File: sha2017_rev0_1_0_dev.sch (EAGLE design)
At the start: 193 parts, among them IC1 CP210X_USB_UART, IC2 AP7215, IC3 ESP32WROOM32, IC4 MCP73833, IC5 FXL6408, IC6 CPT112, Q1 MOSFET-PCHANNEL, Q2 MMBT2222A, Q3 MMBT2222A, Q4 MMBT2222A, Q5 MMBT2222A, Q6 SI1304 BDL, Q7 MMBT2222A, Q8 MOSFET-PCHANNEL, T1 SI2301DS, X1 JST-PH3, X2 2908-05WB-MG

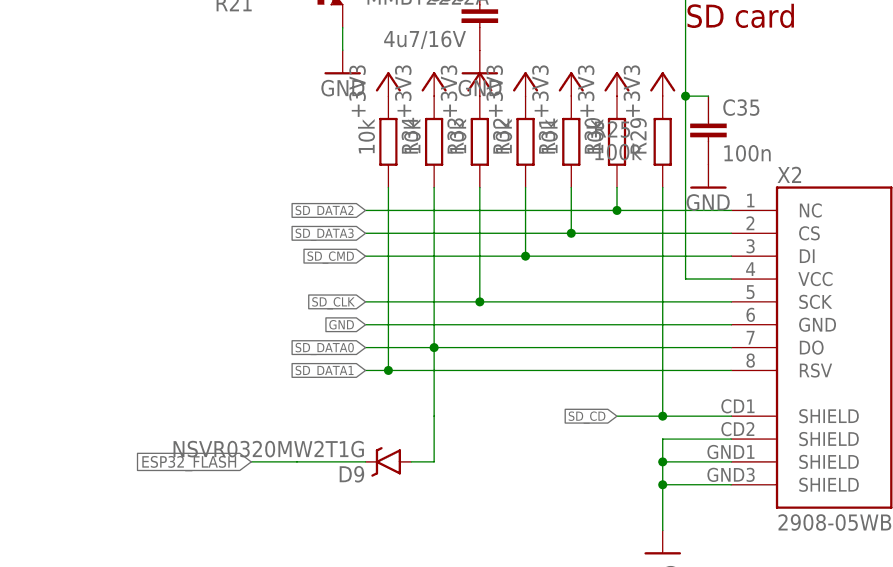
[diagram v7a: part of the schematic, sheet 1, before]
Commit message: add solder briges to unused IOs at 1 Wire SDiomode (roosted: MIMIMI I WANT MORE IOS!!!!!)
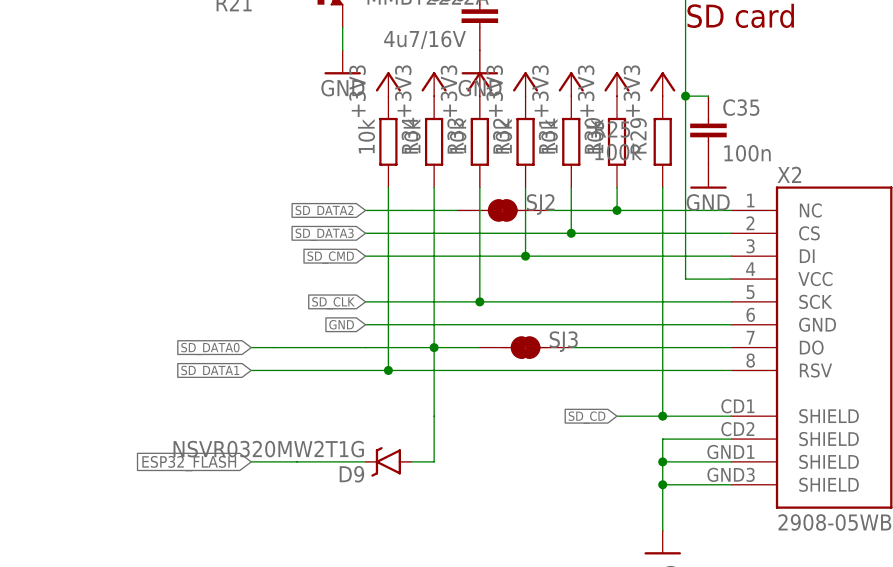
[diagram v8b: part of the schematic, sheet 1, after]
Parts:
- added SJ2, SJ3: JUMPER-PAD-2-NC_BY_TRACE, SparkFun-Passives:JUMPER-PAD-2-NC_BY_TRACE
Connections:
- new net N$20: SJ3.2, X2.DO
- new net SD_DATA2_OUT: R29.1, SJ2.2, X2.NC
- net SD_DATA0: now also SJ3.1; no longer X2.DO
- net SD_DATA2: now also SJ2.1; no longer R29.1, X2.NC
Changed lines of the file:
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@@
 <attribute name="PARTNO" value="BAT20JFILM"/>
 </part>
+<part name="SJ2" library="SparkFun-Passives" deviceset="JUMPER-PAD-2-NC_BY_TRACE" device=""/>
+<part name="SJ3" library="SparkFun-Passives" deviceset="JUMPER-PAD-2-NC_BY_TRACE" device=""/>
 </parts>
 <sheets>
@@
 <attribute name="PARTNO" x="129.54" y="33.02" size="1.778" layer="96" rot="MR270" display="off"/>
 </instance>
+<instance part="SJ2" gate="G$1" x="142.24" y="60.96" smashed="yes">
+<attribute name="NAME" x="144.78" y="60.96" size="1.778" layer="95"/>
+</instance>
+<instance part="SJ3" gate="G$1" x="144.78" y="45.72" smashed="yes">
+<attribute name="NAME" x="147.32" y="45.72" size="1.778" layer="95"/>
+</instance>
 </instances>
 <busses>
@@
 </segment>
 </net>
-<net name="SD_DATA2" class="0">
-<segment>
-<pinref part="X2" gate="G$1" pin="NC"/>
-<wire x1="167.64" y1="60.96" x2="154.94" y2="60.96" width="0.1524" layer="91"/>
-<label x="127" y="60.96" size="1.016" layer="95" rot="R180" xref="yes"/>
-<pinref part="R29" gate="G$1" pin="1"/>
-<wire x1="154.94" y1="60.96" x2="127" y2="60.96" width="0.1524" layer="91"/>
-<wire x1="154.94" y1="63.5" x2="154.94" y2="60.96" width="0.1524" layer="91"/>
-<junction x="154.94" y="60.96"/>
-</segment>
-</net>
 <net name="SD_DATA0" class="0">
 <segment>
-<pinref part="X2" gate="G$1" pin="DO"/>
-<wire x1="167.64" y1="45.72" x2="134.62" y2="45.72" width="0.1524" layer="91"/>
-<label x="127" y="45.72" size="1.016" layer="95" rot="R180" xref="yes"/>
+<wire x1="116.84" y1="45.72" x2="114.3" y2="45.72" width="0.1524" layer="91"/>
+<label x="114.3" y="45.72" size="1.016" layer="95" rot="R180" xref="yes"/>
 <pinref part="R33" gate="G$1" pin="1"/>
+<wire x1="139.7" y1="45.72" x2="134.62" y2="45.72" width="0.1524" layer="91"/>
 <wire x1="134.62" y1="45.72" x2="127" y2="45.72" width="0.1524" layer="91"/>
 <wire x1="134.62" y1="63.5" x2="134.62" y2="45.72" width="0.1524" layer="91"/>
@@
 <wire x1="132.08" y1="33.02" x2="134.62" y2="33.02" width="0.1524" layer="91"/>
 <wire x1="134.62" y1="33.02" x2="134.62" y2="38.1" width="0.1524" layer="91"/>
+<wire x1="116.84" y1="45.72" x2="127" y2="45.72" width="0.1524" layer="91"/>
+<pinref part="SJ3" gate="G$1" pin="1"/>
 </segment>
 </net>
 <net name="SD_DATA1" class="0">
 <segment>
+<wire x1="116.84" y1="43.18" x2="114.3" y2="43.18" width="0.1524" layer="91"/>
+<label x="114.3" y="43.18" size="1.016" layer="95" rot="R180" xref="yes"/>
 <pinref part="X2" gate="G$1" pin="RSV"/>
 <wire x1="167.64" y1="43.18" x2="129.54" y2="43.18" width="0.1524" layer="91"/>
-<label x="127" y="43.18" size="1.016" layer="95" rot="R180" xref="yes"/>
 <pinref part="R34" gate="G$1" pin="1"/>
 <wire x1="129.54" y1="43.18" x2="127" y2="43.18" width="0.1524" layer="91"/>
 <wire x1="129.54" y1="63.5" x2="129.54" y2="43.18" width="0.1524" layer="91"/>
 <junction x="129.54" y="43.18"/>
+<wire x1="116.84" y1="43.18" x2="127" y2="43.18" width="0.1524" layer="91"/>
 </segment>
 </net>
@@
 <pinref part="P+7" gate="VCC" pin="VCC"/>
 <pinref part="R1" gate="G$1" pin="2"/>
+</segment>
+</net>
+<net name="N$20" class="0">
+<segment>
+<pinref part="X2" gate="G$1" pin="DO"/>
+<wire x1="167.64" y1="45.72" x2="149.86" y2="45.72" width="0.1524" layer="91"/>
+<pinref part="SJ3" gate="G$1" pin="2"/>
+</segment>
+</net>
+<net name="SD_DATA2_OUT" class="0">
+<segment>
+<pinref part="X2" gate="G$1" pin="NC"/>
+<wire x1="167.64" y1="60.96" x2="154.94" y2="60.96" width="0.1524" layer="91"/>
+<pinref part="R29" gate="G$1" pin="1"/>
+<wire x1="154.94" y1="60.96" x2="147.32" y2="60.96" width="0.1524" layer="91"/>
+<wire x1="154.94" y1="63.5" x2="154.94" y2="60.96" width="0.1524" layer="91"/>
+<junction x="154.94" y="60.96"/>
+<pinref part="SJ2" gate="G$1" pin="2"/>
+</segment>
+</net>
+<net name="SD_DATA2" class="0">
+<segment>
+<pinref part="SJ2" gate="G$1" pin="1"/>
+<wire x1="137.16" y1="60.96" x2="132.08" y2="60.96" width="0.1524" layer="91"/>
+<wire x1="132.08" y1="60.96" x2="127" y2="60.96" width="0.1524" layer="91"/>
+<label x="127" y="60.96" size="1.016" layer="95" rot="R180" xref="yes"/>
 </segment>
 </net>
@@
 </segment>
 </net>
-<net name="SD_DATA2" class="0">
-<segment>
-<pinref part="IC3" gate="G$1" pin="IO12"/>
-<label x="147.32" y="119.38" size="1.27" layer="95" rot="R180" xref="yes"/>
-<wire x1="147.32" y1="119.38" x2="157.48" y2="119.38" width="0.1524" layer="91"/>
-</segment>
-</net>
 <net name="N$3" class="0">
 <segment>
@@
 </segment>
 </net>
+<net name="SD_DATA2" class="0">
+<segment>
+<pinref part="IC3" gate="G$1" pin="IO12"/>
+<wire x1="157.48" y1="119.38" x2="147.32" y2="119.38" width="0.1524" layer="91"/>
+<label x="147.32" y="119.38" size="1.27" layer="95" rot="R180" xref="yes"/>
+</segment>
+</net>
